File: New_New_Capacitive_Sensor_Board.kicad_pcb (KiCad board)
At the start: 2 copper layers, 22.7 x 21 mm, 13 parts, among them J1 Conn_01x04_Pin, J3 Conn_01x06_Pin, U1 FDC2212QDNTTQ1

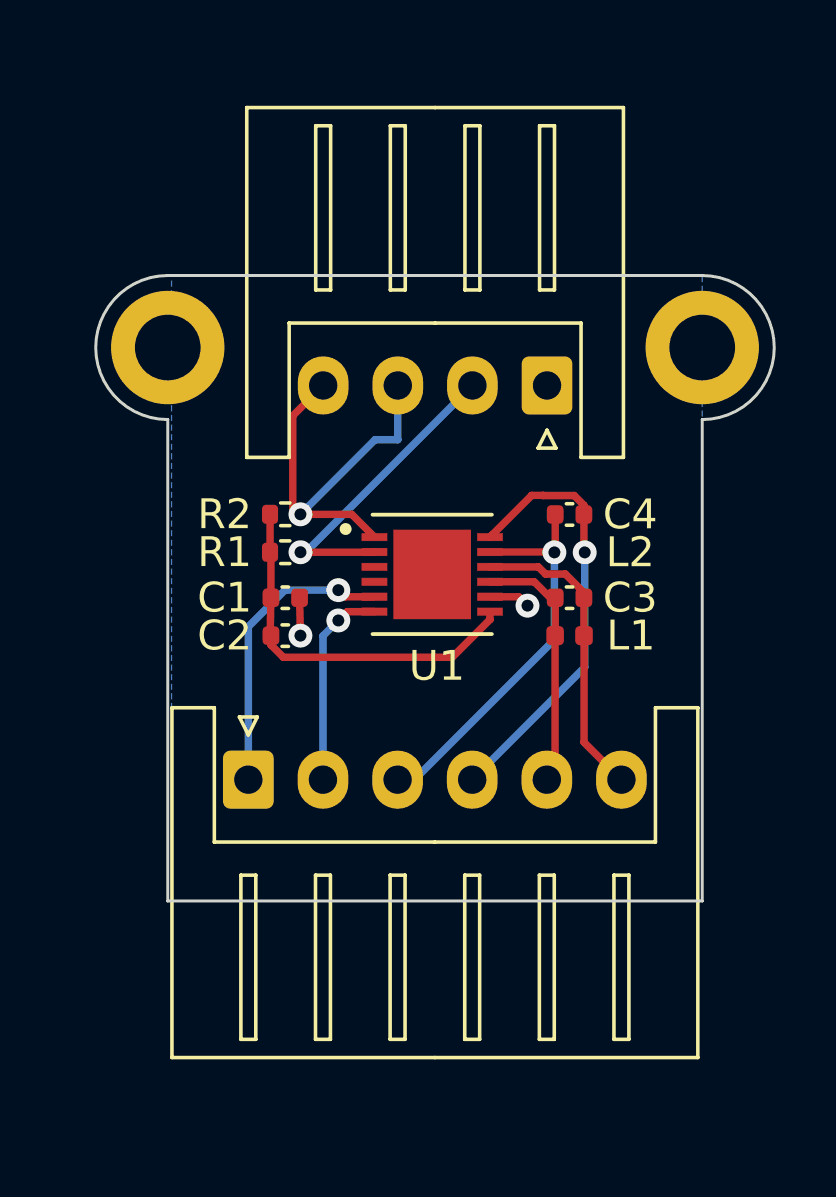
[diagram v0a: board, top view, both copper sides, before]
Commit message: Update PCB Design as per Design Review
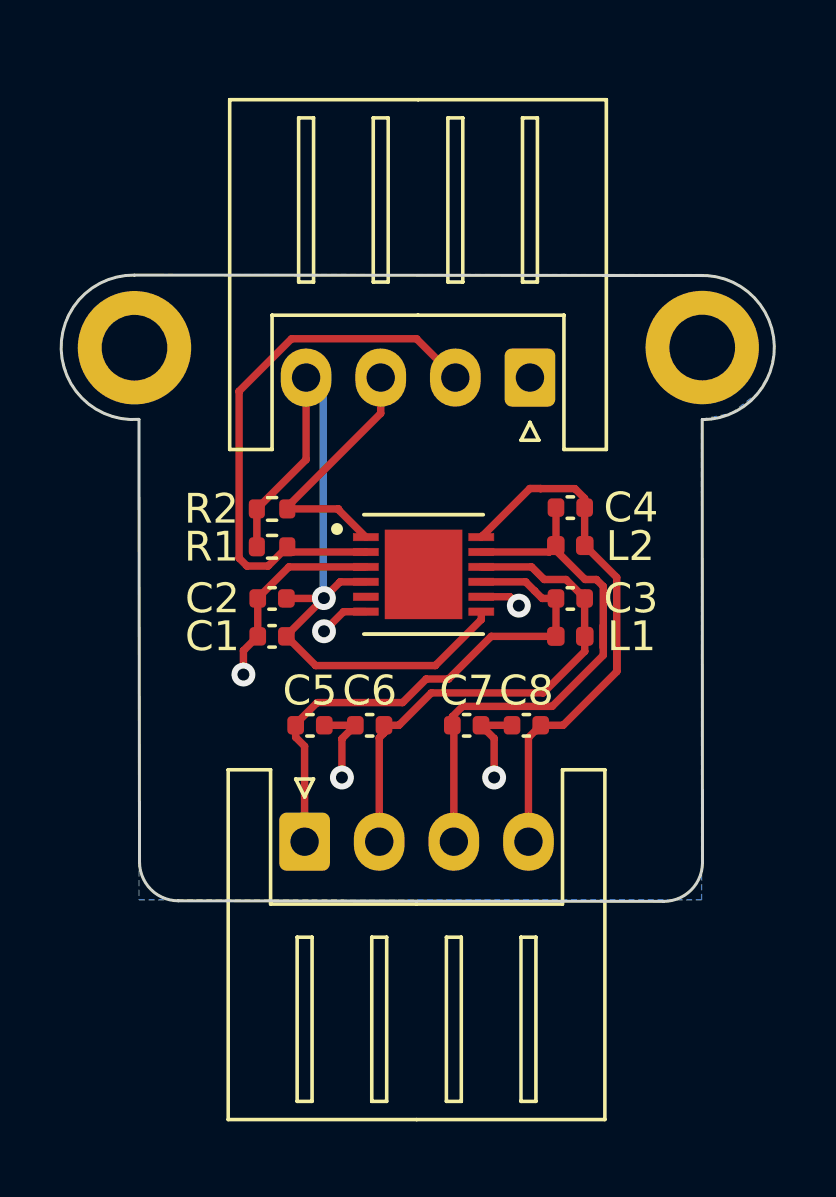
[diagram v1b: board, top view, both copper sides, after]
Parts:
- removed J3: Conn_01x06_Pin, Connector_JST:JST_XH_S6B-XH-A_1x06_P2.50mm_Horizontal
- added C5: 18p, Capacitor_SMD:C_0402_1005Metric, F.Cu at (105.7, 66.2)
- added C6: 18p, Capacitor_SMD:C_0402_1005Metric, F.Cu at (107.7, 66.2)
- added C7: 18p, Capacitor_SMD:C_0402_1005Metric, F.Cu at (111.0, 66.2)
- added C8: 18p, Capacitor_SMD:C_0402_1005Metric, F.Cu at (113.0, 66.2)
- added J2: Conn_01x04_Pin, Connector_JST:JST_XH_S4B-XH-A_1x04_P2.50mm_Horizontal, F.Cu at (105.5, 70.2)
- C2: value 0.1u -> 1u
- moved C1 1.37 mm to (104.5, 63.3), turned to 180 degrees
- moved C2 1.32 mm to (104.5, 62.0), turned to 180 degrees
- moved REF** 1.12 mm to (99.8, 53.6)
- moved J1 0.63 mm to (113.1, 54.6)
- moved R2 0.48 mm to (104.5, 59.0)
- moved R1 0.48 mm to (104.5, 60.3)
- moved U1 0.29 mm to (109.5, 61.2)
- moved L2 0.23 mm to (114.5, 60.2)
- moved C4 0.23 mm to (114.5, 59.0)
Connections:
- U1 pad 3: /CLKIN -> GND
- U1 pad 5: INTB -> unconnected-(U1-INTB-Pad5)
- U1 pad 6: SD -> GND
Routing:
- net GND: track 2.68 -> 15.8 mm, vias 2 -> 5
- net INTB: track 9.95 -> 0.00 mm, vias 1 -> 0
- net IN0A: track 8.62 -> 18.0 mm
- net VDD: track 17.5 -> 25.7 mm, vias 0 -> 1
- net SD: track 7.85 -> 0.00 mm, vias 1 -> 0
- net SDA: track 11.4 -> 18.8 mm, vias 1 -> 0
- net IN0B: track 10.3 -> 17.6 mm
- net IN1A: track 13.6 -> 19.6 mm, vias 1 -> 0
- net IN1B: track 14.8 -> 19.1 mm, vias 1 -> 0
- net SCL: track 8.92 -> 8.74 mm, vias 1 -> 0
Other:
- board size 22.7 x 21 mm -> 23.9 x 21 mm
- copper layers 2 -> 4

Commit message: Remove harsh trace angles
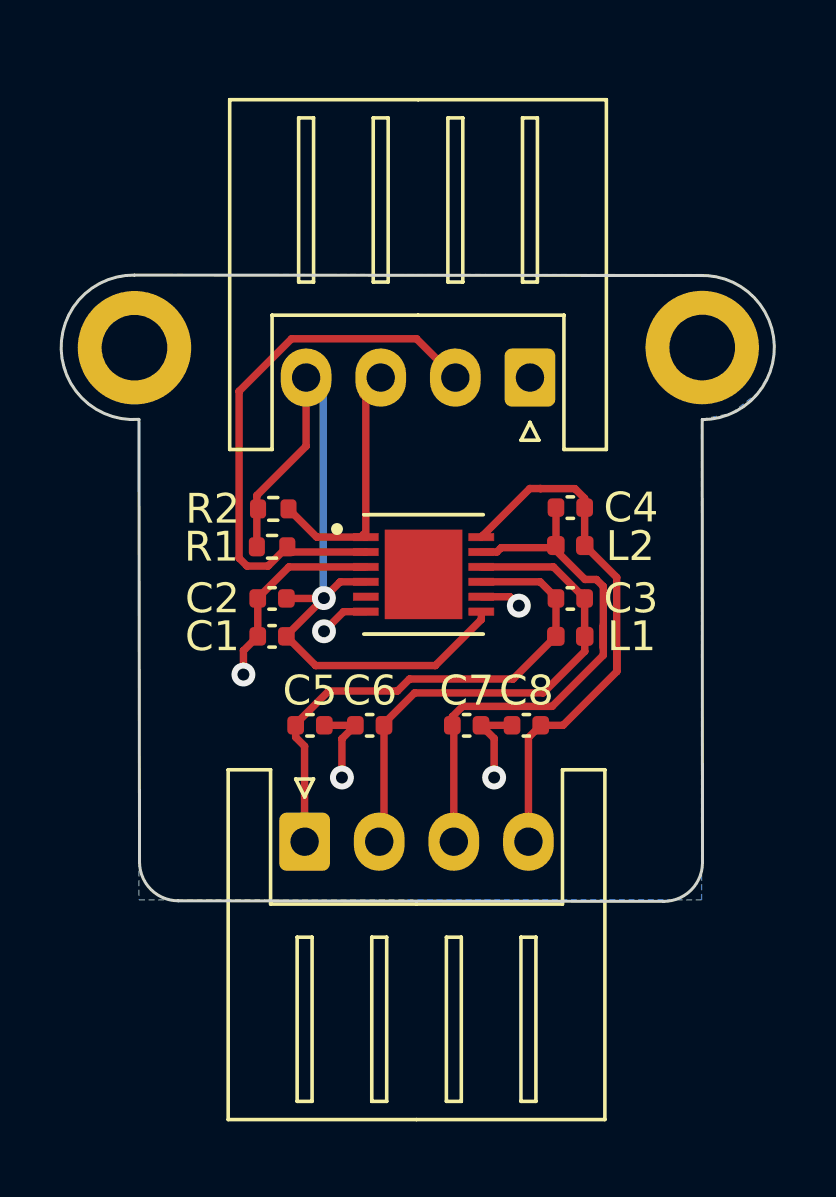
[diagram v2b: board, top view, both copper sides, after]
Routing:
- net SCL: track 8.74 -> 9.49 mm
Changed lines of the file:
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@@
 	(footprint "Resistor_SMD:R_0402_1005Metric"
 		(layer "F.Cu")
-		(at 104.46 59 180)
+		(at 104.5 59 180)
 		(descr "Resistor SMD 0402 (1005 Metric), square (rectangular) end terminal, IPC_7351 nominal, (Body size source: IPC-SM-782 page 72, https://www.pcb-3d.com/wordpress/wp-content/uploads/ipc-sm-782a_amendment_1_and_2.pdf), generated with kicad-footprint-generator")
 		(tags "resistor")
@@
 	)
 	(segment
-		(start 104.94 63.27)
-		(end 104.94 63.244693)
+		(start 105.6 56.9)
+		(end 103.95 58.55)
 		(width 0.25)
 		(layer "F.Cu")
@@
 	)
 	(segment
-		(start 109.929 64.25)
-		(end 105.92 64.25)
+		(start 103.95 58.55)
+		(end 103.95 60.27)
 		(width 0.25)
 		(layer "F.Cu")
@@
 	)
 	(segment
-		(start 103.95 59)
-		(end 103.95 60.27)
+		(start 104.94 63.27)
+		(end 104.94 63.244693)
 		(width 0.25)
 		(layer "F.Cu")
@@
 	)
 	(segment
-		(start 106.184693 62)
-		(end 106.196286 61.988407)
+		(start 109.929 64.25)
+		(end 105.92 64.25)
 		(width 0.25)
 		(layer "F.Cu")
@@
 	)
 	(segment
-		(start 105.6 54.6)
-		(end 105.6 57.35)
+		(start 106.184693 62)
+		(end 106.196286 61.988407)
 		(width 0.25)
 		(layer "F.Cu")
@@
 	)
 	(segment
-		(start 104.94 63.244693)
-		(end 106.196286 61.988407)
+		(start 105.6 54.6)
+		(end 105.6 56.9)
 		(width 0.25)
 		(layer "F.Cu")
@@
 	)
 	(segment
-		(start 111.47 62.709)
-		(end 109.929 64.25)
+		(start 104.94 63.244693)
+		(end 106.196286 61.988407)
 		(width 0.25)
 		(layer "F.Cu")
@@
 	)
 	(segment
-		(start 105.6 57.35)
-		(end 103.95 59)
+		(start 111.47 62.709)
+		(end 109.929 64.25)
 		(width 0.25)
 		(layer "F.Cu")
@@
 	)
 	(segment
-		(start 113.510299 62)
-		(end 113.972 62)
+		(start 105.25 66.21)
+		(end 105.25 66.25)
 		(width 0.25)
 		(layer "F.Cu")
@@
 	)
 	(segment
-		(start 113.256299 61.746)
-		(end 113.510299 62)
+		(start 105.25 66.65)
+		(end 105.55 66.95)
 		(width 0.25)
 		(layer "F.Cu")
@@
 	)
 	(segment
-		(start 105.969999 65.490001)
-		(end 105.25 66.21)
+		(start 108.663604 65.1)
+		(end 106.36 65.1)
 		(width 0.25)
 		(layer "F.Cu")
@@
 	)
 	(segment
-		(start 105.25 66.65)
-		(end 105.55 66.95)
+		(start 106.36 65.1)
+		(end 105.25 66.21)
 		(width 0.25)
 		(layer "F.Cu")
@@
 	)
 	(segment
-		(start 112.954299 61.444)
-		(end 113.256299 61.746)
+		(start 113.967 63.27)
+		(end 112.537 64.7)
 		(width 0.25)
 		(layer "F.Cu")
@@
 	)
 	(segment
-		(start 109.623604 64.7)
-		(end 108.833603 65.490001)
+		(start 112.537 64.7)
+		(end 109.063604 64.7)
 		(width 0.25)
 		(layer "F.Cu")
@@
 	)
 	(segment
-		(start 108.833603 65.490001)
-		(end 105.969999 65.490001)
+		(start 109.063604 64.7)
+		(end 108.663604 65.1)
 		(width 0.25)
 		(layer "F.Cu")
@@
 	)
 	(segment
-		(start 111.803604 63.27)
-		(end 110.373604 64.7)
+		(start 113.444 61.444)
+		(end 113.972 61.972)
 		(width 0.25)
 		(layer "F.Cu")
@@
 	)
 	(segment
-		(start 110.373604 64.7)
-		(end 109.623604 64.7)
+		(start 113.972 61.972)
+		(end 113.972 62)
 		(width 0.25)
 		(layer "F.Cu")
@@
 	)
 	(segment
-		(start 105.55 66.95)
-		(end 105.55 70.15)
+		(start 111.47 61.444)
+		(end 113.444 61.444)
 		(width 0.25)
 		(layer "F.Cu")
@@
 	)
 	(segment
-		(start 113.967 63.27)
-		(end 111.803604 63.27)
+		(start 105.55 66.95)
+		(end 105.55 70.15)
 		(width 0.25)
 		(layer "F.Cu")
@@
 	)
 	(segment
-		(start 105.25 66.21)
-		(end 105.25 66.25)
-		(width 0.25)
-		(layer "F.Cu")
-		(net 3)
-	)
-	(segment
-		(start 111.47 61.444)
-		(end 112.954299 61.444)
-		(width 0.25)
-		(layer "F.Cu")
-		(net 3)
-	)
-	(segment
 		(start 114.932 63.265)
 		(end 114.937 63.27)
@@
 	)
 	(segment
-		(start 114.937 63.773)
-		(end 114.937 63.27)
-		(width 0.25)
-		(layer "F.Cu")
-		(net 4)
-	)
-	(segment
-		(start 114.932 62)
-		(end 114.932 63.265)
-		(width 0.25)
-		(layer "F.Cu")
-		(net 4)
-	)
-	(segment
-		(start 114.30849 61.365)
-		(end 114.932 61.98851)
+		(start 114.932 61.98851)
+		(end 114.932 62)
 		(width 0.25)
 		(layer "F.Cu")
@@
 	)
 	(segment
-		(start 108.21 66.25)
-		(end 108.21 66.51)
+		(start 109.235 65.165)
+		(end 113.545 65.165)
 		(width 0.25)
 		(layer "F.Cu")
@@
 	)
 	(segment
-		(start 108.21 66.25)
-		(end 108.71 66.25)
+		(start 111.47 60.944)
+		(end 113.88749 60.944)
 		(width 0.25)
 		(layer "F.Cu")
@@
 	)
 	(segment
-		(start 114.932 61.98851)
-		(end 114.932 62)
+		(start 113.545 65.165)
+		(end 114.937 63.773)
 		(width 0.25)
 		(layer "F.Cu")
@@
 	)
 	(segment
-		(start 113.575 61.365)
-		(end 114.30849 61.365)
+		(start 114.932 62)
+		(end 114.932 63.265)
 		(width 0.25)
 		(layer "F.Cu")
@@
 	)
 	(segment
-		(start 111.47 60.944)
-		(end 113.154 60.944)
+		(start 108.21 66.25)
+		(end 108.21 66.19)
 		(width 0.25)
 		(layer "F.Cu")
@@
 	)
 	(segment
-		(start 108.71 66.25)
-		(end 109.795 65.165)
+		(start 108.21 66.25)
+		(end 108.21 69.99)
 		(width 0.25)
 		(layer "F.Cu")
@@
 	)
 	(segment
-		(start 108.21 66.51)
-		(end 108.05 66.67)
+		(start 108.21 66.19)
+		(end 109.235 65.165)
 		(width 0.25)
 		(layer "F.Cu")
@@
 	)
 	(segment
-		(start 109.795 65.165)
-		(end 113.545 65.165)
+		(start 114.932 61.828848)
+		(end 114.932 62)
 		(width 0.25)
 		(layer "F.Cu")
@@
 	)
 	(segment
-		(start 113.545 65.165)
-		(end 114.937 63.773)
+		(start 108.21 69.99)
+		(end 108.05 70.15)
 		(width 0.25)
 		(layer "F.Cu")
@@
 	)
 	(segment
-		(start 114.932 61.828848)
-		(end 114.932 62)
+		(start 114.937 63.773)
+		(end 114.937 63.27)
 		(width 0.25)
 		(layer "F.Cu")
@@
 	)
 	(segment
-		(start 108.05 66.67)
-		(end 108.05 70.15)
+		(start 113.88749 60.944)
+		(end 114.932 61.98851)
 		(width 0.25)
 		(layer "F.Cu")
@@
 	)
 	(segment
-		(start 113.154 60.944)
-		(end 113.575 61.365)
+		(start 112.1341 60.3)
+		(end 113.894 60.3)
 		(width 0.25)
 		(layer "F.Cu")
-		(net 4)
+		(net 5)
 	)
 	(segment
@@
 	)
 	(segment
-		(start 111.47 60.444)
-		(end 113.75 60.444)
-		(width 0.25)
-		(layer "F.Cu")
-		(net 5)
-	)
-	(segment
 		(start 114.944886 61.365)
 		(end 115.325 61.365)
@@
 	)
 	(segment
+		(start 111.9901 60.444)
+		(end 112.1341 60.3)
+		(width 0.25)
+		(layer "F.Cu")
+		(net 5)
+	)
+	(segment
 		(start 113.967 60.387114)
 		(end 114.944886 61.365)
@@
 	)
 	(segment
-		(start 113.75 60.444)
+		(start 113.894 60.3)
 		(end 113.967 60.227)
 		(width 0.25)
@@
 	)
 	(segment
+		(start 111.47 60.444)
+		(end 111.9901 60.444)
+		(width 0.25)
+		(layer "F.Cu")
+		(net 5)
+	)
+	(segment
 		(start 111.47 59.944)
 		(end 111.5335 59.8805)
@@
 	)
 	(segment
-		(start 107.6 60.444)
-		(end 107.592 60.452)
+		(start 105.144 60.444)
+		(end 107.6 60.444)
 		(width 0.25)
 		(layer "F.Cu")
@@
 	)
 	(segment
-		(start 104.97 60.27)
-		(end 105.144 60.444)
+		(start 107.6 60.444)
+		(end 107.592 60.452)
 		(width 0.25)
 		(layer "F.Cu")
@@
 	)
 	(segment
-		(start 105.144 60.444)
-		(end 107.6 60.444)
+		(start 104.97 60.27)
+		(end 105.144 60.444)
 		(width 0.25)
 		(layer "F.Cu")
@@
 	)
 	(segment
-		(start 104.968 58.998)
-		(end 104.97 59)
-		(width 0.25)
-		(layer "F.Cu")
-		(net 8)
-	)
-	(segment
-		(start 106.686 59.03)
-		(end 107.6 59.944)
-		(width 0.25)
-		(layer "F.Cu")
-		(net 8)
-	)
-	(segment
-		(start 104.968 59)
-		(end 104.968 58.998)
+		(start 105.954 59.944)
+		(end 105.01 59)
 		(width 0.25)
 		(layer "F.Cu")
@@
 	)
 	(segment
-		(start 106.686 59)
-		(end 106.686 59.03)
+		(start 107.6 59.944)
+		(end 105.954 59.944)
 		(width 0.25)
 		(layer "F.Cu")
@@
 	)
 	(segment
-		(start 104.97 59)
-		(end 104.968 59)
-		(width 0.25)
-		(layer "F.Cu")
-		(net 8)
-	)
-	(segment
-		(start 104.97 58.93)
-		(end 108.1 55.8)
+		(start 107.51 55.19)
+		(end 108.1 54.6)
 		(width 0.25)
 		(layer "F.Cu")
@@
 	)
 	(segment
-		(start 104.97 59)
-		(end 106.686 59)
+		(start 108.1 54.6)
+		(end 107.6 55.1)
 		(width 0.25)
 		(layer "F.Cu")
@@
 	)
 	(segment
-		(start 104.97 59)
-		(end 104.97 58.93)
+		(start 107.6 55.1)
+		(end 107.6 59.944)
 		(width 0.25)
 		(layer "F.Cu")
@@
 	)
 	(segment
-		(start 108.1 55.8)
-		(end 108.1 54.6)
+		(start 107.51 59.854)
+		(end 107.6 59.944)
 		(width 0.25)
 		(layer "F.Cu")

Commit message: needs gerber files
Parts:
- removed C1: 0.1u, Capacitor_SMD:C_0402_1005Metric
- removed C2: 1u, Capacitor_SMD:C_0402_1005Metric
- removed R1, R2: 1k, Resistor_SMD:R_0402_1005Metric
- removed REF** (x2): MountingHole_2.2mm_M2_DIN965_Pad, MountingHole:MountingHole_2.2mm_M2_DIN965_Pad
- removed U1: FDC2212QDNTTQ1, AD7150BRMZ:SON50P400X400X100-13N
- added C10: 1u, Capacitor_SMD:C_0402_1005Metric, F.Cu at (105.3, 63.2)
- added C9: 0.1u, Capacitor_SMD:C_0402_1005Metric, F.Cu at (106.7, 63.1)
- added G***: LOGO, iclr:nocap, B.Cu at (109.5, 62.4)
- added H1: MountingHole, MountingHole:MountingHole_3.2mm_M3_DIN965, F.Cu at (103.5, 59.5)
- added H2: MountingHole, MountingHole:MountingHole_3.2mm_M3_DIN965, F.Cu at (115.0, 59.5)
- added IC1: FDC2212QDNTTQ1, iclr:SON50P400X400X100-13N, F.Cu at (109.1, 60.0)
- added R3: 1k, Resistor_SMD:R_0402_1005Metric, F.Cu at (111.2, 56.9)
- added R4: 1k, Resistor_SMD:R_0402_1005Metric, F.Cu at (109.2, 56.9)
- L1, L2: footprint Inductor_SMD:L_0402_1005Metric -> Inductor_SMD:L_1210_3225Metric
- moved L1 7.71 mm to (107.3, 66.1)
- moved L2 6.42 mm to (111.8, 66.1)
- moved C3 5.92 mm to (108.6, 63.1)
- moved C4 5.76 mm to (110.5, 63.1)
- moved C5 2.45 mm to (106.8, 64.0), turned to 180 degrees
- moved C6 2.39 mm to (108.6, 64.0), turned to 180 degrees
- moved C8 2.31 mm to (112.3, 64.0), turned to 180 degrees
- moved C7 2.27 mm to (110.5, 64.0), turned to 180 degrees
- moved J1 0.98 mm to (113.2, 53.6)
- moved J2 0.43 mm to (105.8, 70.5)
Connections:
- net IN0A renamed IN0+
- net IN0B renamed IN0-
- net IN1A renamed IN1+
- net IN1B renamed IN1-
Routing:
- net SDA: track 18.8 -> 4.82 mm
- net IN1+: track 19.6 -> 9.06 mm
- net IN1-: track 19.1 -> 9.78 mm
- net GND: track 15.8 -> 6.78 mm, vias 5 -> 63
- net IN0-: track 17.6 -> 9.08 mm
- net IN0+: track 18.0 -> 9.78 mm
- net VDD: track 25.7 -> 17.6 mm, vias 1 -> 2
- net SCL: track 9.49 -> 10.3 mm
- added copper zone on F.Cu, net GND
- added copper zone on F.Cu, net VDD
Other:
- board size 23.9 x 21 mm -> 18.5 x 36 mm
- copper layers 4 -> 2
- board text added: "+"
- board text added: "-"
- board text added: "CH0"
- board text added: "CH1"
- board text added: "Designed by Toby Browne Electronics 2024"
- board text added: "SCL"
- board text added: "SDA"
